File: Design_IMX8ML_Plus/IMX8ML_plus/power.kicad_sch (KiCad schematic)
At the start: 9 parts, among them U4 PCA9450CHNY, Y1 32.768KHz

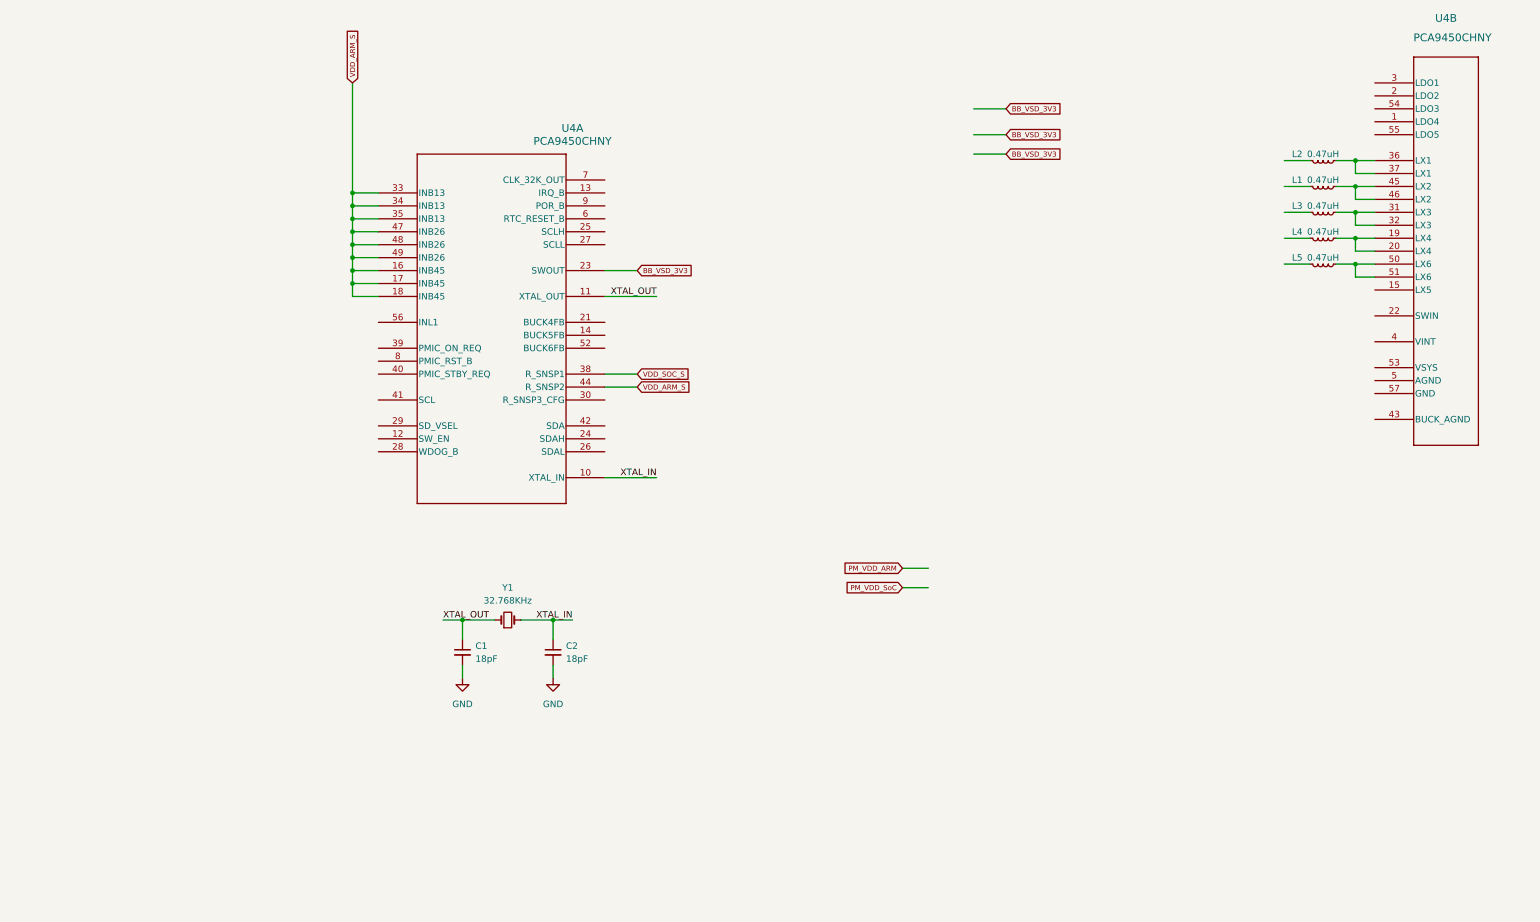
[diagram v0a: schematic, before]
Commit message: Add resistors to PMIC
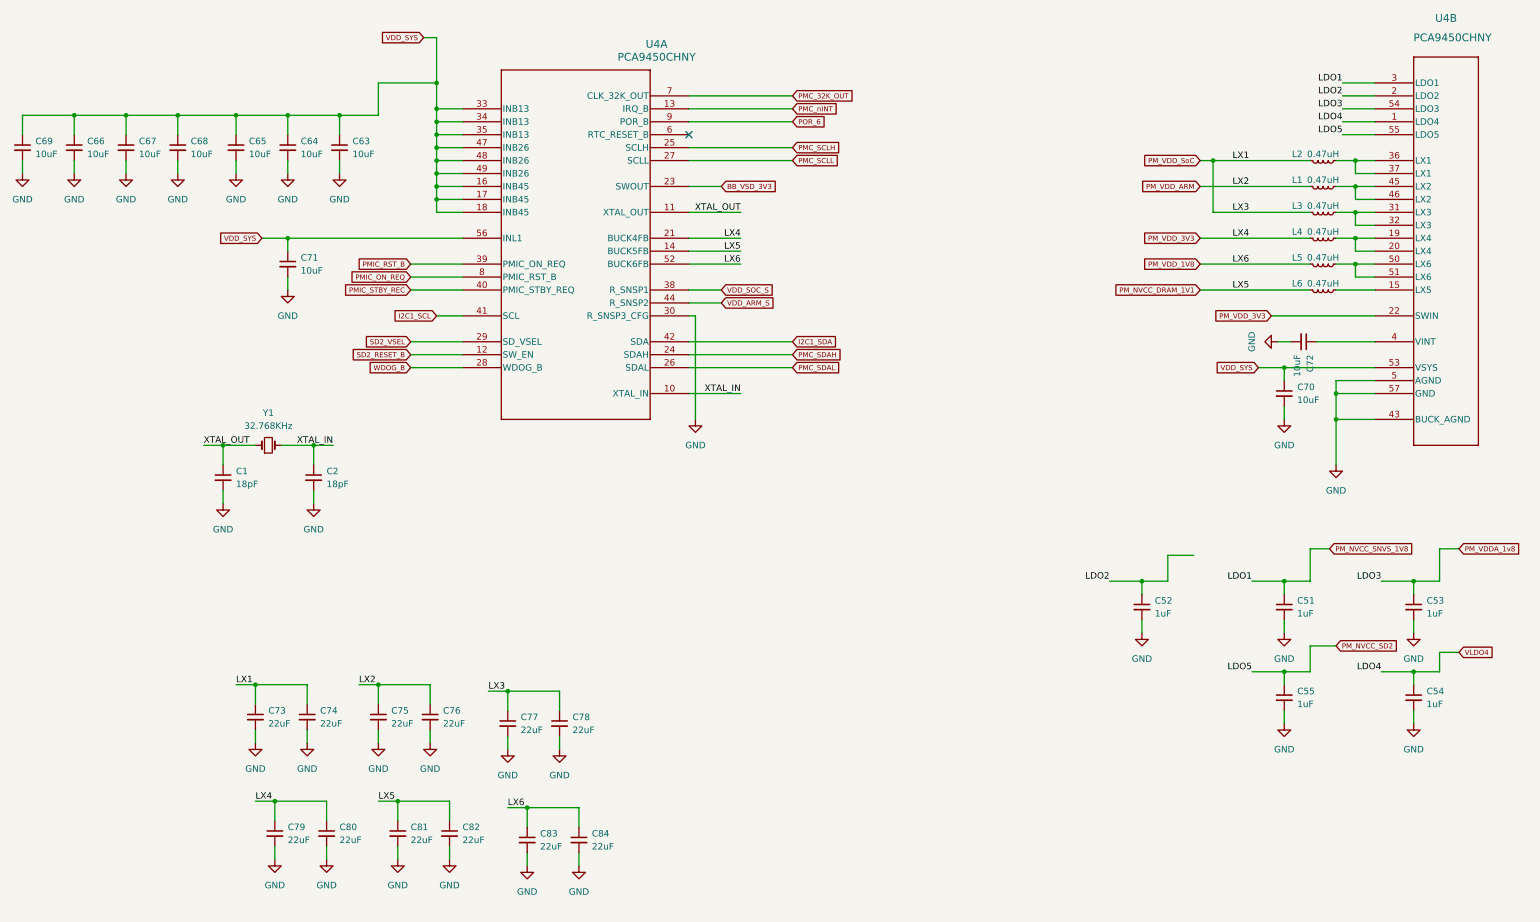
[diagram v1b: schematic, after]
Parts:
- added C51, C52, C53, C54, C55: 1uF, Capacitor_SMD:C_0201_0603Metric_Pad0.64x0.40mm_HandSolder, symbol Device:C_Small
- added C63, C64, C65, C66, C67, C68, C69, C71: 10uF, Capacitor_SMD:C_0603_1608Metric_Pad1.08x0.95mm_HandSolder, symbol Device:C_Small
- added C70, C72: 10uF, Capacitor_SMD:C_0402_1005Metric_Pad0.74x0.62mm_HandSolder, symbol Device:C_Small
- added C73, C74, C75, C76, C77, C78, C79, C80, C81, C82, C83, C84: 22uF, Capacitor_SMD:C_0603_1608Metric_Pad1.08x0.95mm_HandSolder, symbol Device:C_Small
- added L6: 0.47uH, Inductor_SMD:L_0805_2012Metric_Pad1.05x1.20mm_HandSolder, symbol Device:L_Small
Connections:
- net GND: now also U4.30 (R_SNSP3_CFG), U4.43 (BUCK_AGND), U4.5 (AGND), U4.57 (GND), C51.2, C52.2, C53.2, C54.2, C55.2, C63.2, C64.2, C65.2, C66.2, C67.2, C68.2, C69.2, C70.2, C71.2, C72.2, C73.2, C74.2, C75.2, C76.2, C77.2, C78.2, C79.2, C80.2, C81.2, C82.2, C83.2, C84.2
- net PM_VDD_ARM: now also L1.2, C75.1, C76.1
- net PM_VDD_SoC: now also L2.2, L3.2, C73.1, C74.1, C77.1, C78.1
- net VDD_ARM_S: no longer U4.16 (INB45), U4.17 (INB45), U4.18 (INB45), U4.33 (INB13), U4.34 (INB13), U4.35 (INB13), U4.47 (INB26), U4.48 (INB26), U4.49 (INB26)
- net PM_VDD_1V8: now reaches L5.2
- net PM_VDD_1V8: now also U4.52 (BUCK6FB), C83.1, C84.1
- net SD2_RESET_B: now reaches U4.12 (SW_EN)
- net PMC_nINT: now reaches U4.13 (IRQ_B)
- net PM_NVCC_DRAM_1V1: now reaches U4.14 (BUCK5FB)
- net PM_NVCC_DRAM_1V1: now also C81.1, C82.1, L6.2
- net PM_VDD_3V3: now reaches U4.21 (BUCK4FB)
- net PM_VDD_3V3: now also L4.2, U4.22 (SWIN), C79.1, C80.1
- net PMC_SDAH: now reaches U4.24 (SDAH)
- net PMC_SCLH: now reaches U4.25 (SCLH)
- net PMC_SDAL: now reaches U4.26 (SDAL)
- net PMC_SCLL: now reaches U4.27 (SCLL)
- net WDOG_B: now reaches U4.28 (WDOG_B)
- net SD2_VSEL: now reaches U4.29 (SD_VSEL)
- net PMIC_RST_B: now reaches U4.39 (PMIC_ON_REQ)
- net PMIC_STBY_REC: now reaches U4.40 (PMIC_STBY_REQ)
- net I2C1_SCL: now reaches U4.41 (SCL)
- net I2C1_SDA: now reaches U4.42 (SDA)
- net VDD_SYS: now reaches U4.56 (INL1)
- net VDD_SYS: now also U4.16 (INB45), U4.17 (INB45), U4.18 (INB45), U4.33 (INB13), U4.34 (INB13), U4.35 (INB13), U4.47 (INB26), U4.48 (INB26), U4.49 (INB26), U4.53 (VSYS), C63.1, C64.1, C65.1, C66.1, C67.1, C68.1, C69.1, C70.1, C71.1
- net PMC_32K_OUT: now reaches U4.7 (CLK_32K_OUT)
- net PMIC_ON_REQ: now reaches U4.8 (PMIC_RST_B)
- net POR_6: now reaches U4.9 (POR_B)
- net VLDO4: now reaches U4.1 (LDO4)
- net VLDO4: now also C54.1
- net at U4.15 (LX5): now also L6.1
- net LDO2: now reaches U4.2 (LDO2)
- net LDO2: now also C52.1
- net PM_NVCC_SNVS_1V8: now reaches U4.3 (LDO1)
- net PM_NVCC_SNVS_1V8: now also C51.1
- net at U4.4 (VINT): now also C72.1
- net PM_VDDA_1v8: now reaches U4.54 (LDO3)
- net PM_VDDA_1v8: now also C53.1
- net PM_NVCC_SD2: now reaches U4.55 (LDO5)
- net PM_NVCC_SD2: now also C55.1
- no-connect marks 0 -> 1
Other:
- moved on the sheet: C1, C2, U4A, Y1

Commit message: Add interface io pins
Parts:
- added R2: 100K, Resistor_SMD:R_0402_1005Metric_Pad0.72x0.64mm_HandSolder, symbol Device:R_Small
- U4: footprint _W_SBC:DHX2QFN18_SOT1442-1_NXP-L -> _W_SBC:HVQFN56_SOT949-6_NXP-M
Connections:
- net PMIC_ON_REQ: now also U4.39 (PMIC_ON_REQ); no longer U4.8 (PMIC_RST_B)
- net PMIC_RST_B: now also U4.8 (PMIC_RST_B), R2.2; no longer U4.39 (PMIC_ON_REQ)
- net PM_NVCC_DRAM_1V1: now also C83.1, C84.1, L5.2, U4.52 (BUCK6FB); no longer C81.1, C82.1, L6.2, U4.14 (BUCK5FB)
- net PM_VDD_1V8: now also C81.1, C82.1, L6.2, U4.14 (BUCK5FB); no longer C83.1, C84.1, L5.2, U4.52 (BUCK6FB)
- net PM_VDDA_1v8 renamed PM_VDDA_1V8
- net VDD_SOC_S renamed VDD_SoC_S
- new net NVCC_SNVS_1V8: R2.1
- no-connect marks 1 -> 2
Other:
- moved on the sheet: C1, C2, C63, C64, C65, C66, C67, C68, C69, C71, U4A, Y1

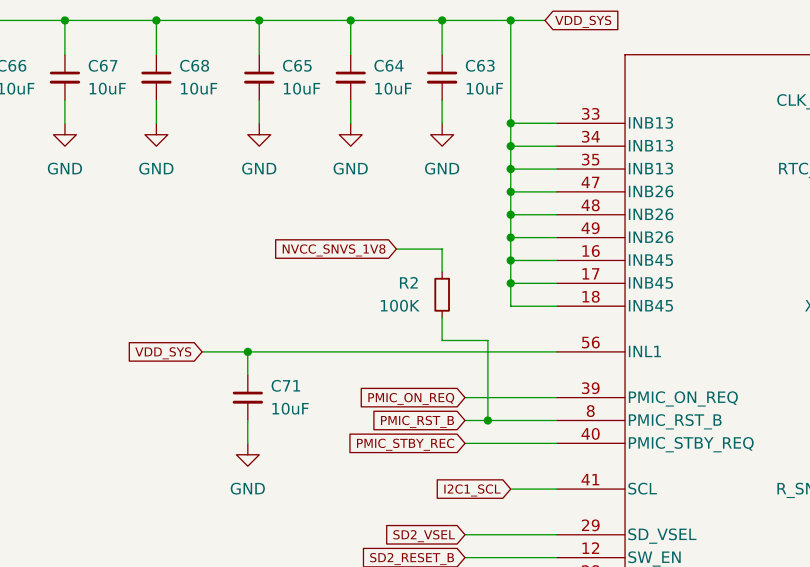
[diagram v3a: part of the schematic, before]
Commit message: Add SPB228 WIFI/BLE module
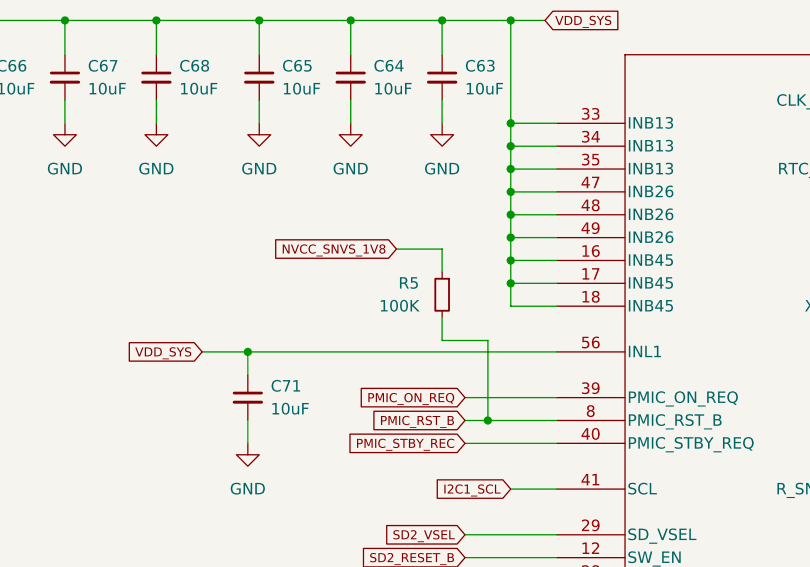
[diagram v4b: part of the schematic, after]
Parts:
- renumbered R2 to R5

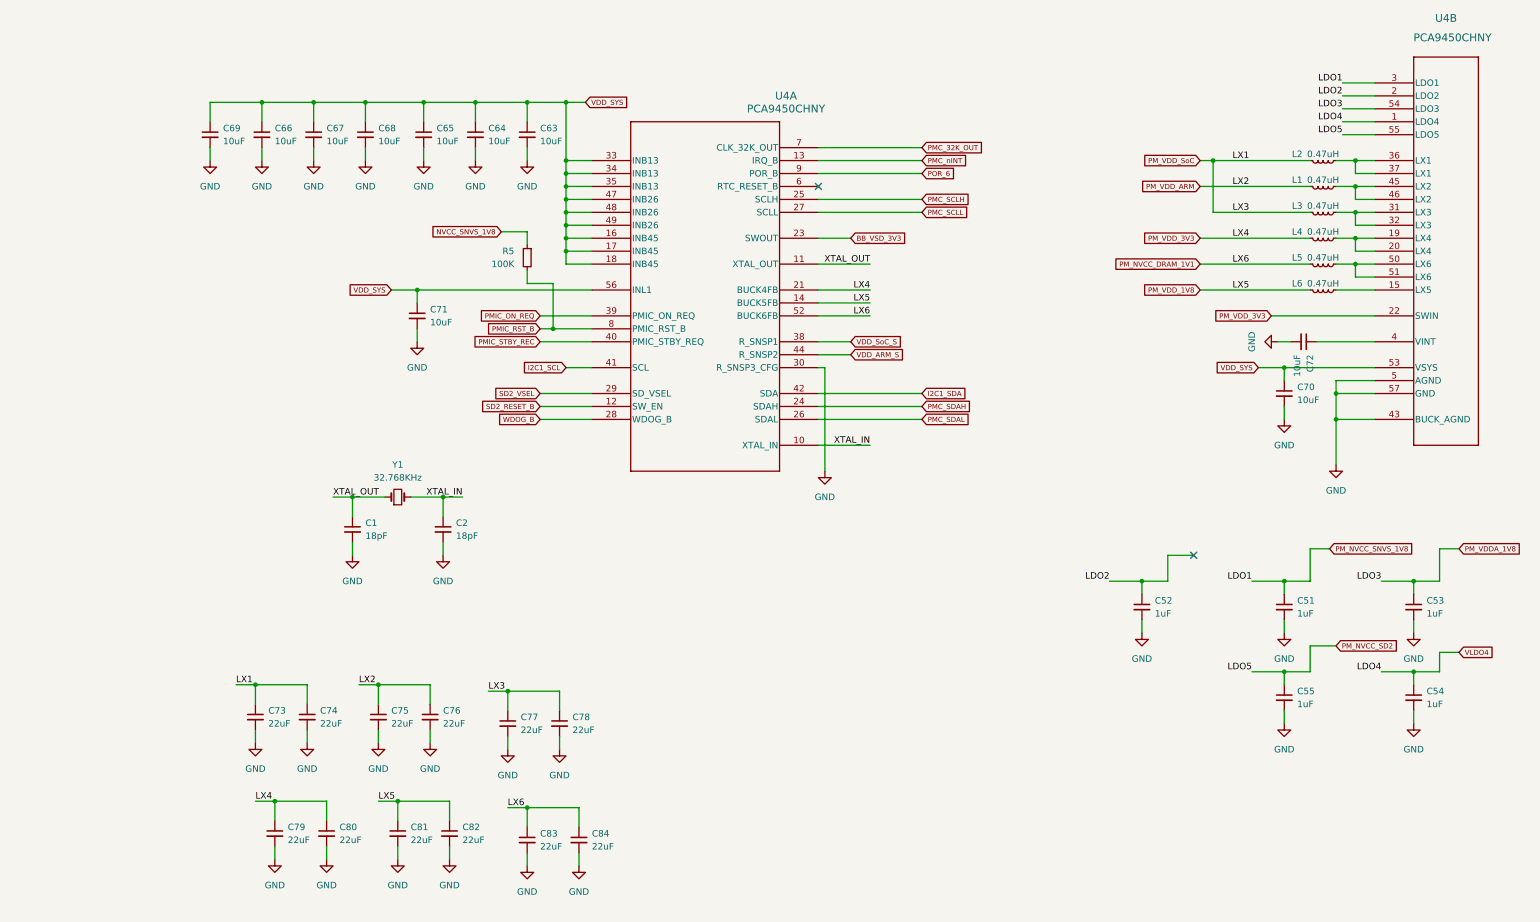
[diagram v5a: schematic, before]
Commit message: [PROCESSOR] Create zones It added power zones in the four layer
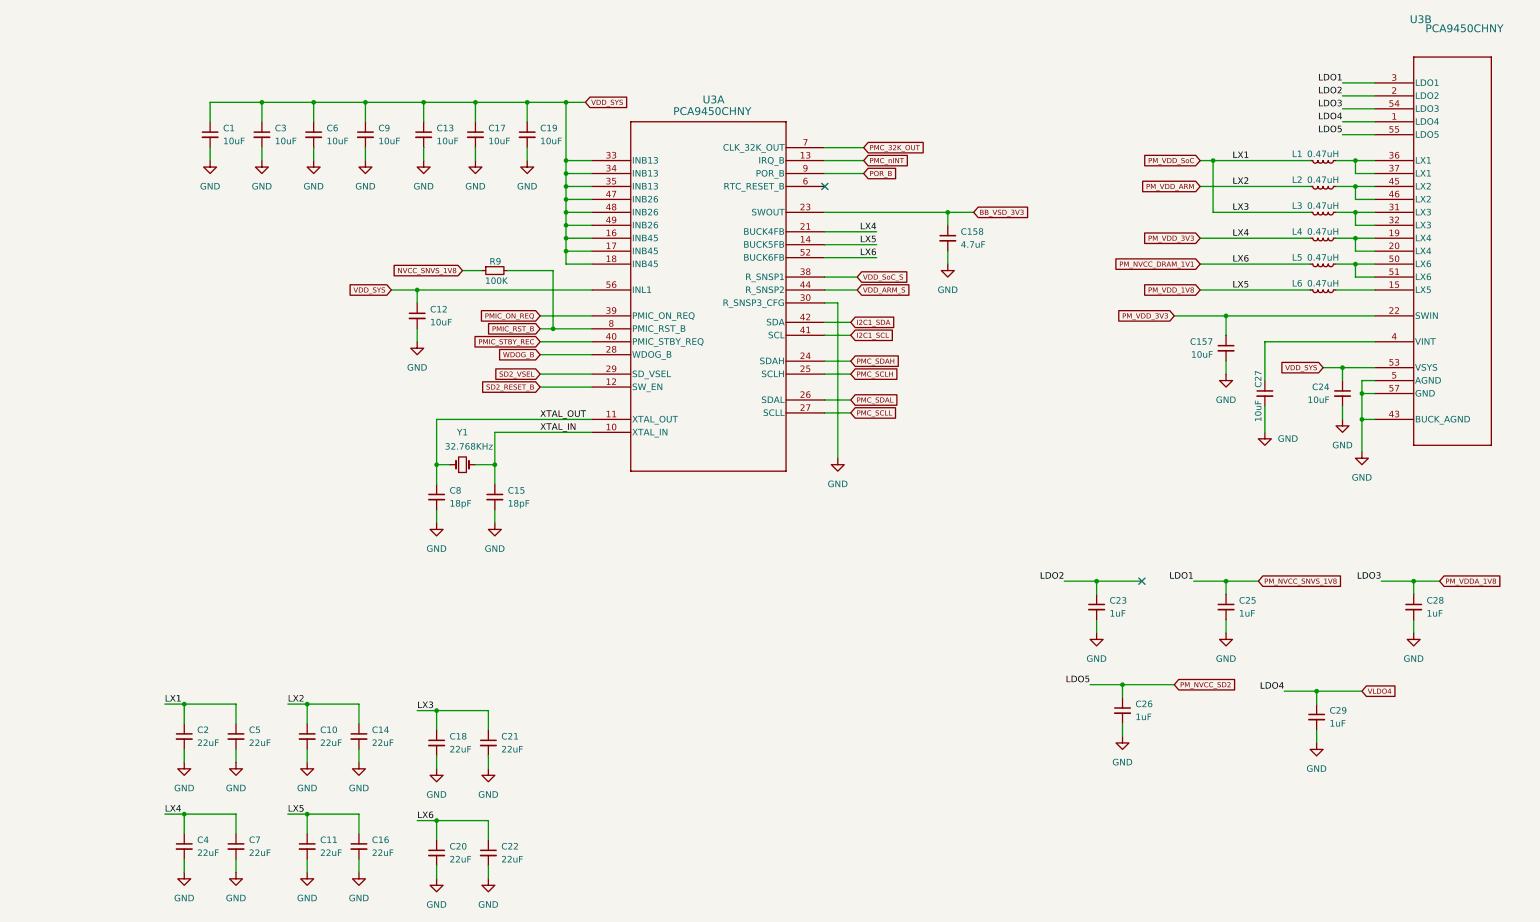
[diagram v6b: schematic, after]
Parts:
- removed U4: PCA9450CHNY, _W_SBC:HVQFN56_SOT949-6_NXP-M, symbol pca9450_NXP:PCA9450CHNY
- added C157: 10uF, Capacitor_SMD:C_0603_1608Metric_Pad1.08x0.95mm_HandSolder, symbol Device:C_Small
- added C158: 4.7uF, Capacitor_SMD:C_0402_1005Metric, symbol Device:C_Small
- added U3: PCA9450CHNY, HVQFN56_SOT949-6_NXP, symbol PCA9450CHNY:PCA9450CHNY
- L1: renamed from L2; footprint Inductor_SMD:L_0805_2012Metric_Pad1.05x1.20mm_HandSolder -> Inductor_SMD:L_APV_ANR252012
- L2: renamed from L1; footprint Inductor_SMD:L_0805_2012Metric_Pad1.05x1.20mm_HandSolder -> Inductor_SMD:L_APV_ANR252012
- L3, L4: footprint Inductor_SMD:L_0805_2012Metric_Pad1.05x1.20mm_HandSolder -> Inductor_SMD:L_APV_ANR252012
- L5, L6: footprint Inductor_SMD:L_0805_2012Metric_Pad1.05x1.20mm_HandSolder -> Inductor_SMD:L_Cenker_CKCS201610
- Y1: footprint Crystal:Crystal_SMD_0603-2Pin_6.0x3.5mm_HandSoldering -> Crystal:Crystal_SMD_3215-2Pin_3.2x1.5mm
- renumbered C69 to C1, C75 to C10, C81 to C11, C71 to C12, C65 to C13, C76 to C14, C2 to C15, C82 to C16, C64 to C17, C77 to C18, C63 to C19, C73 to C2, C83 to C20, C78 to C21, C84 to C22, C52 to C23, C70 to C24, C51 to C25, C55 to C26, C72 to C27, C53 to C28, C54 to C29, C66 to C3, C79 to C4, C74 to C5, C67 to C6, C80 to C7, C1 to C8, C68 to C9, R5 to R9
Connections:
- net BB_VSD_3V3: now also C158.1, U3.23 (SWOUT)
- net GND: now also C157.2, C158.2, U3.30 (R_SNSP3_CFG), U3.43 (BUCK_AGND), U3.5 (AGND), U3.57 (GND)
- net I2C1_SCL: now also U3.41 (SCL)
- net I2C1_SDA: now also U3.42 (SDA)
- net LDO2: now also U3.2 (LDO2)
- net PMC_32K_OUT: now also U3.7 (CLK_32K_OUT)
- net PMC_SCLH: now also U3.25 (SCLH)
- net PMC_SCLL: now also U3.27 (SCLL)
- net PMC_SDAH: now also U3.24 (SDAH)
- net PMC_SDAL: now also U3.26 (SDAL)
- net PMC_nINT: now also U3.13 (IRQ_B)
- net PMIC_ON_REQ: now also U3.39 (PMIC_ON_REQ)
- net PMIC_RST_B: now also U3.8 (PMIC_RST_B)
- net PMIC_STBY_REC: now also U3.40 (PMIC_STBY_REQ)
- net PM_NVCC_DRAM_1V1: now also U3.52 (BUCK6FB)
- net PM_NVCC_SD2: now also U3.55 (LDO5)
- net PM_NVCC_SNVS_1V8: now also U3.3 (LDO1)
- net PM_VDDA_1V8: now also U3.54 (LDO3)
- net PM_VDD_1V8: now also U3.14 (BUCK5FB)
- net PM_VDD_3V3: now also C157.1, U3.21 (BUCK4FB), U3.22 (SWIN)
- net SD2_RESET_B: now also U3.12 (SW_EN)
- net SD2_VSEL: now also U3.29 (SD_VSEL)
- net VDD_ARM_S: now also U3.44 (R_SNSP2)
- net VDD_SYS: now also U3.16 (INB45), U3.17 (INB45), U3.18 (INB45), U3.33 (INB13), U3.34 (INB13), U3.35 (INB13), U3.47 (INB26), U3.48 (INB26), U3.49 (INB26), U3.53 (VSYS), U3.56 (INL1)
- net VDD_SoC_S: now also U3.38 (R_SNSP1)
- net VLDO4: now also U3.1 (LDO4)
- net WDOG_B: now also U3.28 (WDOG_B)
- net XTAL_IN: now also U3.10 (XTAL_IN)
- net XTAL_OUT: now also U3.11 (XTAL_OUT)
- net at L3.1: now also U3.31 (LX3), U3.32 (LX3)
- net at L5.1: now also U3.50 (LX6), U3.51 (LX6)
- net at C27.1: now also U3.4 (VINT)
- net at L6.1: now also U3.15 (LX5)
- net at L4.1: now also U3.19 (LX4), U3.20 (LX4)
- net at L2.1: now also U3.45 (LX2), U3.46 (LX2)
- net at L1.1: now also U3.36 (LX1), U3.37 (LX1)
- new net POR_B: U3.9 (POR_B)
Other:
- moved on the sheet: C10, C11, C14, C15, C16, C18, C2, C20, C21, C22, C23, C24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

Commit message: [BB_IMX8MLP IMX8MLP] Actuallizated to 9.0 kicad version
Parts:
- C1, C12, C13, C157, C17, C19, C3, C6, C9: footprint Capacitor_SMD:C_0603_1608Metric_Pad1.08x0.95mm_HandSolder -> Capacitor_SMD:C_0603_1608Metric; MP (none) -> GRT188R61C106KE13D; Price (none) -> 0.4
- C10, C11, C14, C16, C18, C2, C20, C21, C22, C4, C5, C7: footprint Capacitor_SMD:C_0603_1608Metric_Pad1.08x0.95mm_HandSolder -> Capacitor_SMD:C_0603_1608Metric; MP (none) -> C1608X5R1A226M080AC; Price (none) -> 0.3
- C15, C8: footprint Capacitor_SMD:C_0201_0603Metric_Pad0.64x0.40mm_HandSolder -> Capacitor_SMD:C_0201_0603Metric; MP (none) -> GRM0335C1H180JA01D; Price (none) -> 0.1
- C158: MP (none) -> C1005X5R0J475M050BC; Price (none) -> 0.4
- C23, C25, C26, C28, C29: footprint Capacitor_SMD:C_0201_0603Metric_Pad0.64x0.40mm_HandSolder -> Capacitor_SMD:C_0201_0603Metric; MP (none) -> 02016D105MAT2A; Price (none) -> 0.1
- C24, C27: footprint Capacitor_SMD:C_0402_1005Metric_Pad0.74x0.62mm_HandSolder -> Capacitor_SMD:C_0402_1005Metric; MP (none) -> CL05A106MQ5NUNC; Price (none) -> 0.1
- L1, L2, L3, L4: MP (none) -> WPN252012ER47MT; Price (none) -> ND
- L5, L6: MP (none) -> WPN252012HR47MT; Price (none) -> ND
- R9: footprint Resistor_SMD:R_0402_1005Metric_Pad0.72x0.64mm_HandSolder -> Resistor_SMD:R_0402_1005Metric
- U3: footprint HVQFN56_SOT949-6_NXP -> _W_SBC:HVQFN56_SOT949-6_NXP; MP (none) -> -
- Y1: MP (none) -> ABS07-32.768KHZ-7-T; Price (none) -> 1

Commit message: [IMX8ML] Add new layer
A new layers was add in the cpu schematic, now it had 8 layer.
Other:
- note added: "LX1 = VDD_SoC LX2 = VDD_ARM LX3 = LX1 LX4 = NVCC_3V3 LX5 = NVCC_1V88 LX6 = NVCC_DRAM SWOUT =SD_CARD LDO1 = NVCC_SNVS LDO2 = X LDO3 = VDDA LDO4 LDO5 = NVCC_SDA"
- note added: "PMIC_ON_REQ [39] Porcessor/PinOUT SYS_nRST [8] PinOUT PMIC_STBY_REQ [40] Processor PMCNnINT [13] Processor(GPIO) WDOG_B [28] Processor(GPIO)/PinOUT POR_B [9] Processor/PinOUT"
- note added: "VSD_3v3"
